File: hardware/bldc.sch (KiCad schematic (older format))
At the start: 6 parts, among them J1 U_OUT, J2 V_OUT, J3 W_OUT, U1 7805

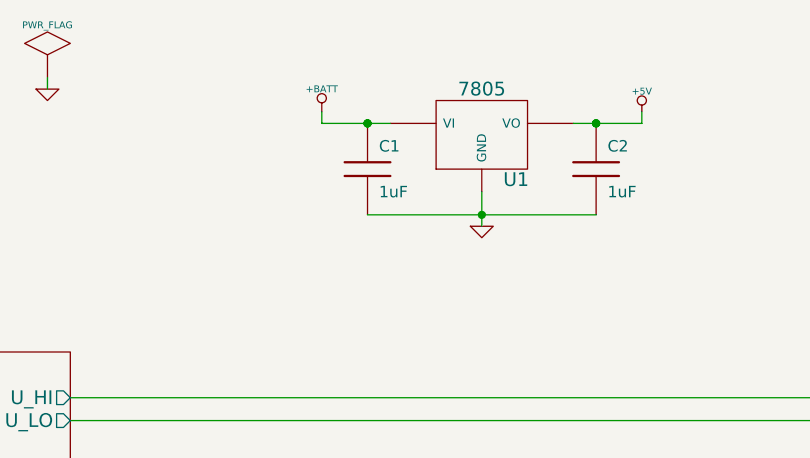
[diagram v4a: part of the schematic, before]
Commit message: Added inital layout revision.
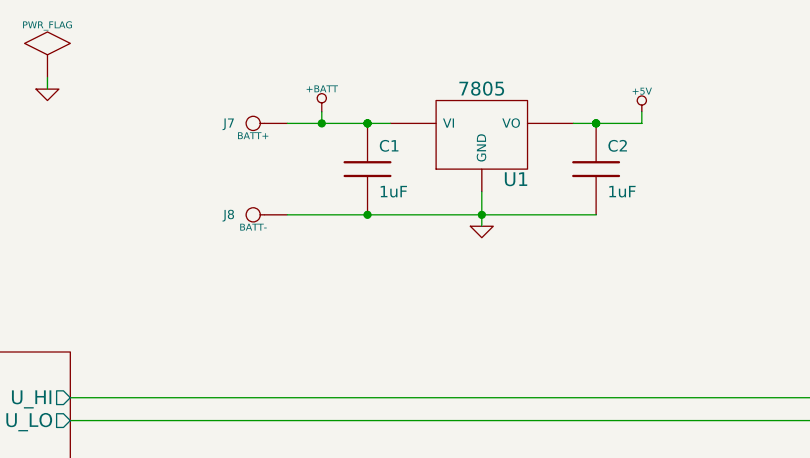
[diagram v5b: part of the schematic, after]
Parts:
- added J7: BATT+, symbol CONN_1
- added J8: BATT-, symbol CONN_1
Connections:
- net +BATT: now also J7.1
- net GND: now also J8.1
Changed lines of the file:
@@
-EESchema Schematic File Version 2  date Wed 20 May 2015 21:52:57 MST
+EESchema Schematic File Version 2  date Sun 14 Jun 2015 10:56:58 MST
 LIBS:power
 LIBS:device
@@
 Sheet 1 4
 Title "BLDC Controller"
-Date "21 may 2015"
+Date "14 jun 2015"
 Rev "1"
 Comp ""
@@
 $EndDescr
 $Comp
-L C C2
-U 1 1 555D4F9E
-P 5750 1250
-F 0 "C2" H 5800 1350 50  0000 L CNN
-F 1 "1uF" H 5800 1150 50  0000 L CNN
-F 4 "FK24X7R1H105K" H 5750 1250 60  0001 C CNN "Mfg P/N"
-F 5 "445-8517-ND" H 5750 1250 60  0001 C CNN "Digikey P/N"
-F 6 "810-FK24X7R1H105K" H 5750 1250 60  0001 C CNN "Mouser P/N"
-	1    5750 1250
+L 7805 U1
+U 1 1 557DC005
+P 5250 1100
+F 0 "U1" H 5400 904 60  0000 C CNN
+F 1 "7805" H 5250 1300 60  0000 C CNN
+	1    5250 1100
 	1    0    0    -1
 $EndComp
-$Comp
-L C C1
-U 1 1 555D4F9B
-P 4750 1250
-F 0 "C1" H 4800 1350 50  0000 L CNN
-F 1 "1uF" H 4800 1150 50  0000 L CNN
-F 4 "FK24X7R1H105K" H 4750 1250 60  0001 C CNN "Mfg P/N"
-F 5 "445-8517-ND" H 4750 1250 60  0001 C CNN "Digikey P/N"
-F 6 "810-FK24X7R1H105K" H 4750 1250 60  0001 C CNN "Mouser P/N"
-	1    4750 1250
-	1    0    0    -1
-$EndComp
+Connection ~ 4750 1450
+Wire Wire Line
+	4400 1450 5750 1450
 Wire Wire Line
 	7800 2500 9200 2500
@@
 Connection ~ 5250 1450
 Wire Wire Line
-	5750 1450 4750 1450
-Wire Wire Line
 	5950 1000 5950 1050
 Wire Wire Line
 	5950 1050 5650 1050
-Wire Wire Line
-	4850 1050 4550 1050
 Wire Wire Line
 	4550 1050 4550 1000
@@
 Wire Wire Line
 	9200 2300 7800 2300
+Wire Wire Line
+	4400 1050 4850 1050
+Connection ~ 4550 1050
 $Comp
-L 7805 U1
-U 1 1 554502C3
-P 5250 1100
-F 0 "U1" H 5400 904 60  0000 C CNN
-F 1 "7805" H 5250 1300 60  0000 C CNN
-	1    5250 1100
+L CONN_1 J8
+U 1 1 557DB4F9
+P 4250 1450
+F 0 "J8" H 4330 1450 40  0000 L CNN
+F 1 "BATT-" H 4250 1505 30  0000 C CNN
+	1    4250 1450
+	-1   0    0    1
+$EndComp
+$Comp
+L CONN_1 J7
+U 1 1 557DB4EE
+P 4250 1050
+F 0 "J7" H 4330 1050 40  0000 L CNN
+F 1 "BATT+" H 4250 1105 30  0000 C CNN
+	1    4250 1050
+	-1   0    0    1
+$EndComp
+$Comp
+L C C2
+U 1 1 555D4F9E
+P 5750 1250
+F 0 "C2" H 5800 1350 50  0000 L CNN
+F 1 "1uF" H 5800 1150 50  0000 L CNN
+F 4 "FK24X7R1H105K" H 5750 1250 60  0001 C CNN "Mfg P/N"
+F 5 "445-8517-ND" H 5750 1250 60  0001 C CNN "Digikey P/N"
+F 6 "810-FK24X7R1H105K" H 5750 1250 60  0001 C CNN "Mouser P/N"
+	1    5750 1250
 	1    0    0    -1
 $EndComp
+$Comp
+L C C1
+U 1 1 555D4F9B
+P 4750 1250
+F 0 "C1" H 4800 1350 50  0000 L CNN
+F 1 "1uF" H 4800 1150 50  0000 L CNN
+F 4 "FK24X7R1H105K" H 4750 1250 60  0001 C CNN "Mfg P/N"
+F 5 "445-8517-ND" H 4750 1250 60  0001 C CNN "Digikey P/N"
+F 6 "810-FK24X7R1H105K" H 4750 1250 60  0001 C CNN "Mouser P/N"
+	1    4750 1250
+	1    0    0    -1
+$EndComp

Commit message: Fixed item properties and generated a BOM.
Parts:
- U1: Digikey P/N (none) -> AS78L05ZTR-E1DICT-ND; Mfg P/N (none) -> AS78L05ZTR-E1; Mouser P/N (none) -> 621-AS78L05ZTR-E1
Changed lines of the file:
@@
-EESchema Schematic File Version 2  date Sun 14 Jun 2015 10:56:58 MST
+EESchema Schematic File Version 2  date Sun 14 Jun 2015 15:22:49 MST
 LIBS:power
 LIBS:device
@@
 F 0 "U1" H 5400 904 60  0000 C CNN
 F 1 "7805" H 5250 1300 60  0000 C CNN
+F 3 "datasheets/AS78L05.pdf" H 5250 1100 60  0001 C CNN
+F 4 "AS78L05ZTR-E1" H 5250 1100 60  0001 C CNN "Mfg P/N"
+F 5 "AS78L05ZTR-E1DICT-ND" H 5250 1100 60  0001 C CNN "Digikey P/N"
+F 6 "621-AS78L05ZTR-E1" H 5250 1100 60  0001 C CNN "Mouser P/N"
 	1    5250 1100
 	1    0    0    -1
@@
 $EndSheet
 $Comp
-L GND #PWR01
+L GND #PWR2
 U 1 1 553C10DF
 P 3350 900
-F 0 "#PWR01" H 3350 900 30  0001 C CNN
+F 0 "#PWR2" H 3350 900 30  0001 C CNN
 F 1 "GND" H 3350 830 30  0001 C CNN
 	1    3350 900
@@
 $EndComp
 $Comp
-L PWR_FLAG #FLG02
+L PWR_FLAG #FLG2
 U 1 1 553C10DA
 P 3350 850
-F 0 "#FLG02" H 3350 1120 30  0001 C CNN
+F 0 "#FLG2" H 3350 1120 30  0001 C CNN
 F 1 "PWR_FLAG" H 3350 1080 30  0000 C CNN
 	1    3350 850
@@
 $EndComp
 $Comp
-L PWR_FLAG #FLG03
+L PWR_FLAG #FLG1
 U 1 1 55343C2E
 P 2300 850
-F 0 "#FLG03" H 2300 1120 30  0001 C CNN
+F 0 "#FLG1" H 2300 1120 30  0001 C CNN
 F 1 "PWR_FLAG" H 2300 1080 30  0000 C CNN
 	1    2300 850
@@
 $EndComp
 $Comp
-L +BATT #PWR04
+L +BATT #PWR1
 U 1 1 55343C22
 P 2450 850
-F 0 "#PWR04" H 2450 800 20  0001 C CNN
+F 0 "#PWR1" H 2450 800 20  0001 C CNN
 F 1 "+BATT" H 2450 950 30  0000 C CNN
 	1    2450 850
@@
 $EndSheet
 $Comp
-L GND #PWR05
+L GND #PWR4
 U 1 1 5533EF79
 P 5250 1500
-F 0 "#PWR05" H 5250 1500 30  0001 C CNN
+F 0 "#PWR4" H 5250 1500 30  0001 C CNN
 F 1 "GND" H 5250 1430 30  0001 C CNN
 	1    5250 1500
@@
 $EndComp
 $Comp
-L +BATT #PWR06
+L +BATT #PWR3
 U 1 1 5533EF2A
 P 4550 1000
-F 0 "#PWR06" H 4550 950 20  0001 C CNN
+F 0 "#PWR3" H 4550 950 20  0001 C CNN
 F 1 "+BATT" H 4550 1100 30  0000 C CNN
 	1    4550 1000
@@
 $EndComp
 $Comp
-L +5V #PWR07
+L +5V #PWR5
 U 1 1 5533EF24
 P 5950 1000
-F 0 "#PWR07" H 5950 1090 20  0001 C CNN
+F 0 "#PWR5" H 5950 1090 20  0001 C CNN
 F 1 "+5V" H 5950 1090 30  0000 C CNN
 	1    5950 1000
